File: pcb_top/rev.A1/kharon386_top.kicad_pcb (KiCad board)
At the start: 4 copper layers, 100 x 100 mm, 150 parts, among them J1 PJ-320, J2 Vol. Btns, J3 Conn_02x07_Odd_Even, J4 ESP, J5 PC104_16, J6 PC104, SW1 VGA Config, U1 1117-5.0, U10 93C66A, U11 MT4C4256, U12 MT4C4256, U13 MT4C4256, U14 MT4C4256, U2 NE5532DR, U3 74HCT138PW, U4 ES1868F, U5 TVGA9000I, U6 SAM2695, U7 27C512, U8 1117-5.0, U9 1117-3.3, Y1 40 MHz, Y2 12 MHz

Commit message: wip pcb rev.A1
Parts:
- added C54: 100n, Capacitor_SMD:C_0603_1608Metric_Pad1.08x0.95mm_HandSolder, F.Cu at (126.2, 120.7)
- added R10: 47k, Resistor_SMD:R_0603_1608Metric_Pad0.98x0.95mm_HandSolder, F.Cu at (135.7, 64.3)
- added R12: 47k, Resistor_SMD:R_0603_1608Metric_Pad0.98x0.95mm_HandSolder, F.Cu at (135.7, 60.5)
- moved L4 1.26 mm to (135.7, 62.4)
- moved L5 0.15 mm to (135.7, 58.6)
- turned JP2 to 180 degrees
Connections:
- JP2 pad 1: +5V -> GND
- JP2 pad 3: GND -> +5V
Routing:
- net +5V: track 592.8 -> 595.8 mm, vias 26 -> 27
- net GND: track 208.4 -> 211.4 mm, vias 211 -> 212
- net /AOUT_R: track 3.75 -> 6.32 mm
- net /AOUT_L: track 3.75 -> 5.81 mm
- net Net-(C15-Pad2): track 11.6 -> 11.0 mm

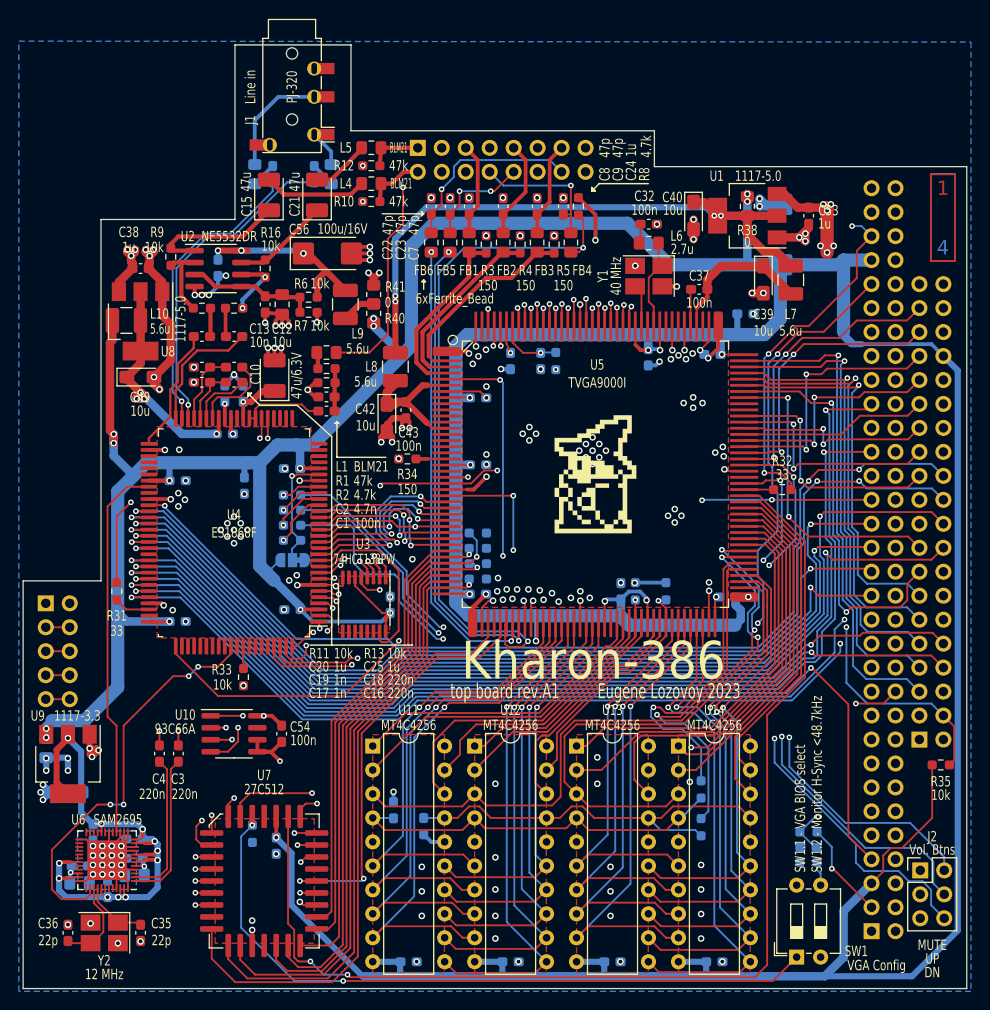
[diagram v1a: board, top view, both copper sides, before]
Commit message: update all pcb rev.A1 files - minor changes
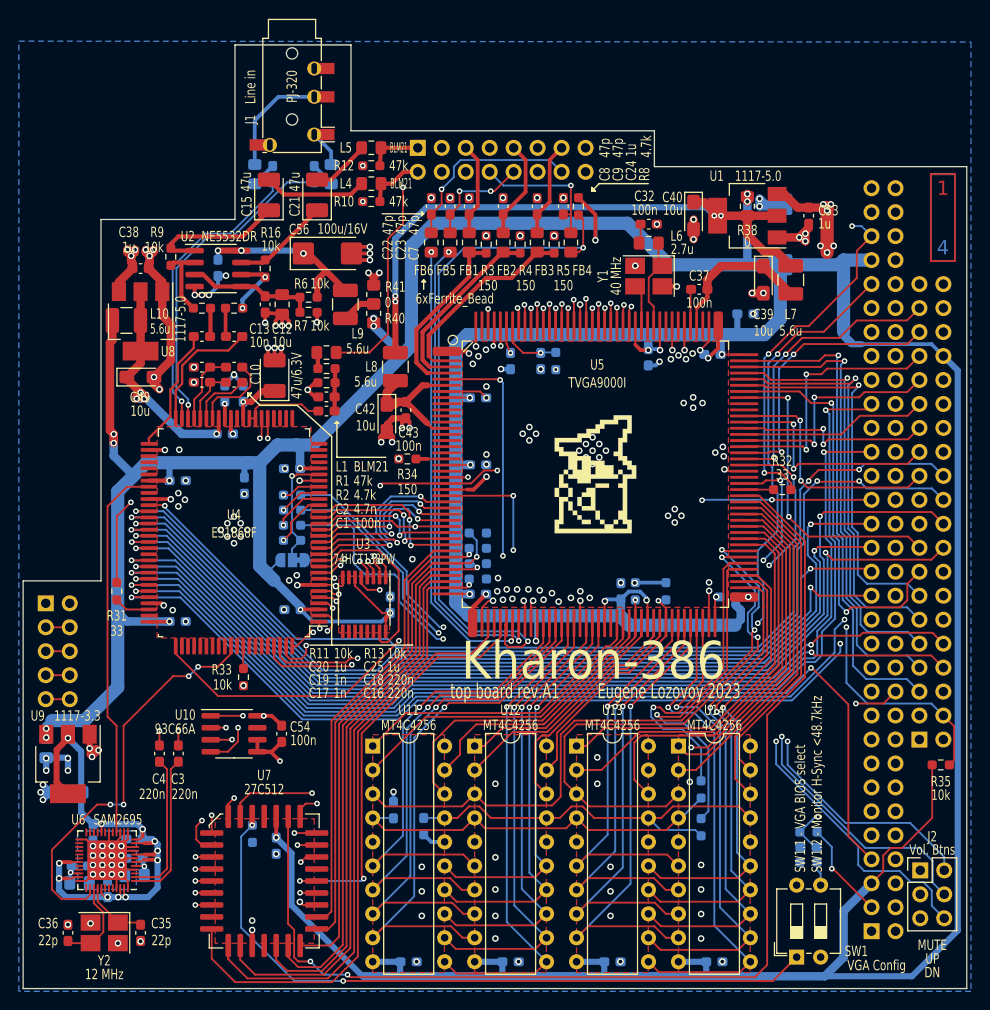
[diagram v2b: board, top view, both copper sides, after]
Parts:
- moved J1 1.28 mm to (127.2, 52.1), turned to 0 degrees
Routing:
- net GND: vias 212 -> 213
- net +5V: vias 27 -> 26
